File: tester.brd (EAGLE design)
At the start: 56 x 67 mm, 71 parts, among them IC1 ATmega8/88/168, K1 NA 05W K, M1 SP6000C-180, P1 250, P2 10k lin, Q1 BC847CSMD, Q2 BC847CSMD, Q3 BC807-40SMD, Q4 8,000 MHz, Q5 BC847CSMD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

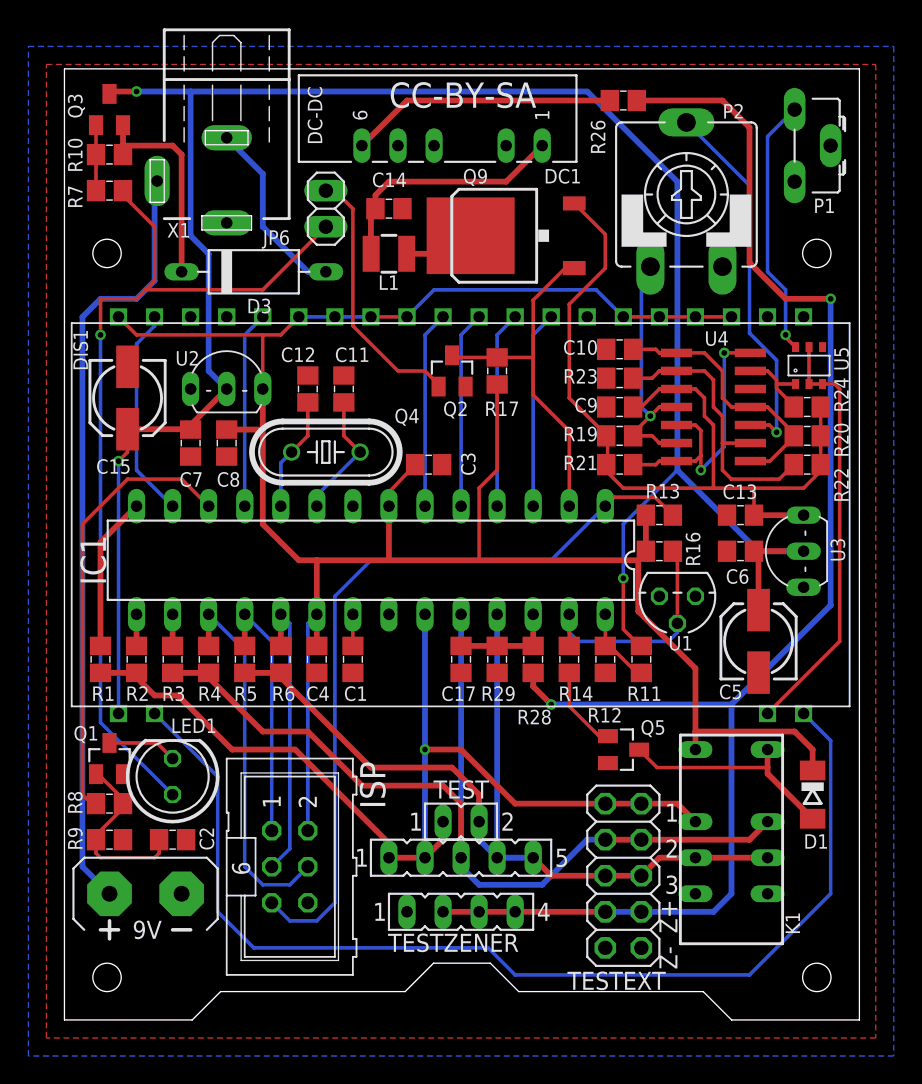
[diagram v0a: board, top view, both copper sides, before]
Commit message: continous part names/numbers
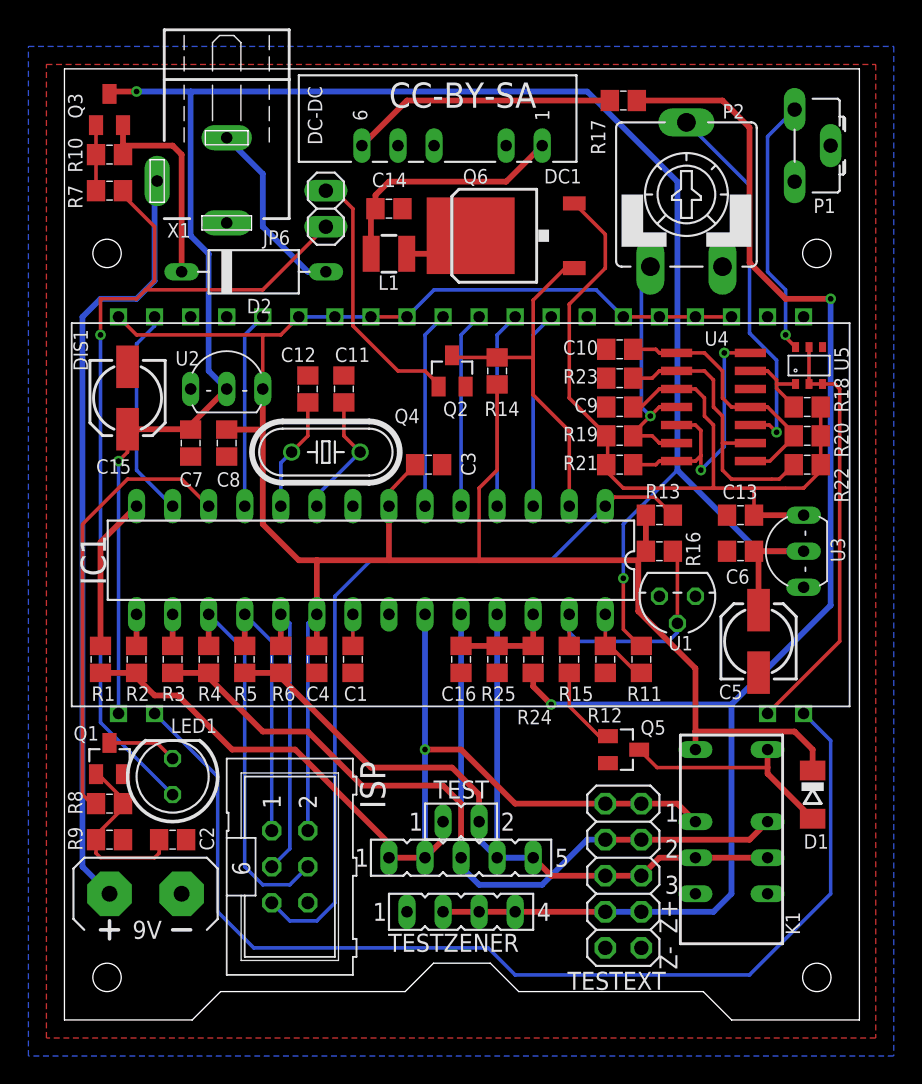
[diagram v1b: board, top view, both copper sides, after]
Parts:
- removed R26: 10k, resistor:R0805
- removed R28: 180k, resistor:R0805
- added R15: 4k7, resistor:R0805
- added R18: 3k3, resistor:R0805
- R14: value 4k7 -> 27k
- R17: value 27k -> 10k
- R24: value 3k3 -> 180k
- moved R24 26.2 mm to (33.0, 25.4), turned to 270 degrees
- moved R17 21.0 mm to (39.4, 64.8), turned to 0 degrees
- moved R14 20.9 mm to (30.5, 45.7)
- renumbered C17 to C16, D3 to D2, Q9 to Q6, R29 to R25
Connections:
- net +30V: now also R17.2, R24.2; no longer R26.2, R28.2
- net +5V: now also R14.2; no longer R17.2
- net +5V/2: now also R18.2; no longer R24.2
- net N$17: now also R18.1; no longer R24.1
- net N$22: now also R15.2; no longer R14.2
- net N$28: now also R17.1; no longer R26.1
- net PC3: now also R24.1; no longer R28.1
- net PC4: now also R15.1; no longer R14.1
- net PD0: now also R14.1; no longer R17.1
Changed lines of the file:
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@@
 <layer number="44" name="Drills" color="7" fill="1" visible="yes" active="yes"/>
 <layer number="45" name="Holes" color="7" fill="1" visible="yes" active="yes"/>
-<layer number="46" name="Milling" color="3" fill="1" visible="no" active="yes"/>
+<layer number="46" name="Milling" color="3" fill="1" visible="yes" active="yes"/>
 <layer number="47" name="Measures" color="7" fill="1" visible="no" active="yes"/>
 <layer number="48" name="Document" color="7" fill="1" visible="no" active="yes"/>
@@
 <attribute name="VALUE" x="8.89" y="41.148" size="1.27" layer="27" ratio="10"/>
 </element>
-<element name="R17" library="resistor" package="R0805" value="27k" x="30.48" y="45.72" smashed="yes" rot="R270">
+<element name="R14" library="resistor" package="R0805" value="27k" x="30.48" y="45.72" smashed="yes" rot="R270">
 <attribute name="NAME" x="29.591" y="42.545" size="1.016" layer="25"/>
 <attribute name="VALUE" x="28.448" y="46.609" size="1.27" layer="27" rot="R270"/>
@@
 <attribute name="VALUE" x="-0.635" y="65.913" size="1.27" layer="27" ratio="10"/>
 </element>
-<element name="D3" library="markus" package="DIODE-3-10" value="SB130" x="13.335" y="52.705" smashed="yes">
+<element name="D2" library="markus" package="DIODE-3-10" value="SB130" x="13.335" y="52.705" smashed="yes">
 <attribute name="NAME" x="14.605" y="50.8" size="1.016" layer="25" rot="R180"/>
 <attribute name="VALUE" x="8.89" y="53.34" size="1.27" layer="27" ratio="10"/>
@@
 <variant name="nopwm" populate="no"/>
 </element>
-<element name="R24" library="resistor" package="R0805" value="3k3" x="52.324" y="43.18" smashed="yes">
+<element name="R18" library="resistor" package="R0805" value="3k3" x="52.324" y="43.18" smashed="yes">
 <attribute name="NAME" x="55.245" y="42.799" size="1.016" layer="25" rot="R90"/>
 <attribute name="VALUE" x="51.435" y="41.148" size="1.27" layer="27"/>
@@
 <attribute name="VALUE" x="36.211" y="20.948" size="1.27" layer="27" rot="R270"/>
 </element>
-<element name="R14" library="resistor" package="R0805" value="4k7" x="35.56" y="25.4" smashed="yes" rot="R270">
+<element name="R15" library="resistor" package="R0805" value="4k7" x="35.56" y="25.4" smashed="yes" rot="R270">
 <attribute name="NAME" x="34.798" y="22.479" size="1.016" layer="25"/>
 <attribute name="VALUE" x="33.528" y="26.289" size="1.27" layer="27" rot="R270"/>
@@
 <attribute name="VALUE" x="52.07" y="24.765" size="1.016" layer="27" rot="R90"/>
 </element>
-<element name="Q9" library="transistor-power" package="D-PAK_TO252AA" value="IRFR9024" x="31.115" y="55.245" smashed="yes" rot="R90">
+<element name="Q6" library="transistor-power" package="D-PAK_TO252AA" value="IRFR9024" x="31.115" y="55.245" smashed="yes" rot="R90">
 <attribute name="NAME" x="28.067" y="58.928" size="1.016" layer="25"/>
 <attribute name="VALUE" x="33.655" y="60.325" size="1.27" layer="27" rot="R180"/>
@@
 <attribute name="VALUE" x="23.368" y="62.865" size="1.27" layer="27" ratio="10"/>
 </element>
-<element name="R26" library="resistor" package="R0805" value="10k" x="39.37" y="64.77" smashed="yes">
+<element name="R17" library="resistor" package="R0805" value="10k" x="39.37" y="64.77" smashed="yes">
 <attribute name="NAME" x="38.1" y="60.96" size="1.016" layer="25" rot="R90"/>
 <attribute name="VALUE" x="38.481" y="62.738" size="1.27" layer="27"/>
 </element>
-<element name="R28" library="resistor" package="R0805" value="180k" x="33.02" y="25.4" smashed="yes" rot="R270">
+<element name="R24" library="resistor" package="R0805" value="180k" x="33.02" y="25.4" smashed="yes" rot="R270">
 <attribute name="TOLERANCE" value="0.1%" x="33.02" y="25.4" size="1.778" layer="27" rot="R270" display="off"/>
 <attribute name="NAME" x="31.877" y="20.828" size="1.016" layer="25"/>
 <attribute name="VALUE" x="30.988" y="26.289" size="1.27" layer="27" rot="R270"/>
 </element>
-<element name="R29" library="resistor" package="R0805" value="20k" x="30.48" y="25.4" smashed="yes" rot="R90">
+<element name="R25" library="resistor" package="R0805" value="20k" x="30.48" y="25.4" smashed="yes" rot="R90">
 <attribute name="TOLERANCE" value="0.1%" x="30.48" y="25.4" size="1.778" layer="27" rot="R90" display="off"/>
 <attribute name="NAME" x="29.337" y="22.479" size="1.016" layer="25"/>
 <attribute name="VALUE" x="32.512" y="24.511" size="1.27" layer="27" rot="R90"/>
 </element>
-<element name="C17" library="rcl" package="C0805" value="10n" x="27.94" y="25.4" smashed="yes" rot="R270">
+<element name="C16" library="rcl" package="C0805" value="10n" x="27.94" y="25.4" smashed="yes" rot="R270">
 <attribute name="NAME" x="26.543" y="22.479" size="1.016" layer="25"/>
 <attribute name="VALUE" x="26.035" y="26.035" size="1.27" layer="27" rot="R270"/>
@@
 <contactref element="C13" pad="2"/>
 <contactref element="C6" pad="2"/>
-<contactref element="R29" pad="1"/>
-<contactref element="C17" pad="2"/>
+<contactref element="R25" pad="1"/>
+<contactref element="C16" pad="2"/>
 <contactref element="JP3" pad="1"/>
 <contactref element="U5" pad="4"/>
@@
 <contactref element="R10" pad="1"/>
 <contactref element="Q3" pad="E"/>
-<contactref element="D3" pad="C"/>
+<contactref element="D2" pad="C"/>
 <wire x1="8.255" y1="52.705" x2="8.255" y2="60.96" width="0.4064" layer="1"/>
 <wire x1="3.81" y1="60.96" x2="4.125" y2="60.96" width="0.4064" layer="1"/>
@@
 <signal name="+5V">
 <contactref element="JP1" pad="2"/>
-<contactref element="R17" pad="2"/>
+<contactref element="R14" pad="2"/>
 <contactref element="C3" pad="2"/>
 <contactref element="R13" pad="1"/>
@@
 </signal>
 <signal name="N$11">
-<contactref element="D3" pad="A"/>
+<contactref element="D2" pad="A"/>
 <contactref element="X1" pad="3"/>
 <wire x1="13.97" y1="59.61" x2="13.97" y2="55.88" width="0.4064" layer="16"/>
@@
 </signal>
 <signal name="N$17">
-<contactref element="R24" pad="1"/>
+<contactref element="R18" pad="1"/>
 <contactref element="U4" pad="13"/>
 <contactref element="U5" pad="1"/>
@@
 </signal>
 <signal name="PC4">
-<contactref element="R14" pad="1"/>
+<contactref element="R15" pad="1"/>
 <contactref element="R16" pad="1"/>
 <contactref element="U1" pad="2"/>
@@
 </signal>
 <signal name="N$22">
-<contactref element="R14" pad="2"/>
+<contactref element="R15" pad="2"/>
 <contactref element="Q5" pad="1"/>
 <wire x1="35.56" y1="24.45" x2="35.56" y2="22.103" width="0.254" layer="1"/>
@@
 </signal>
 <signal name="PC3">
-<contactref element="R29" pad="2"/>
-<contactref element="C17" pad="1"/>
-<contactref element="R28" pad="1"/>
+<contactref element="R25" pad="2"/>
+<contactref element="C16" pad="1"/>
+<contactref element="R24" pad="1"/>
 <contactref element="IC1" pad="26"/>
 <wire x1="30.48" y1="26.35" x2="33.02" y2="26.35" width="0.4064" layer="1"/>
@@
 </signal>
 <signal name="N$24">
-<contactref element="Q9" pad="4"/>
+<contactref element="Q6" pad="4"/>
 <contactref element="L1" pad="1"/>
 <wire x1="28.615" y1="55.245" x2="27.345" y2="53.975" width="0.4064" layer="1"/>
@@
 <signal name="N$28">
 <contactref element="DC1" pad="6"/>
-<contactref element="R26" pad="1"/>
+<contactref element="R17" pad="1"/>
 <wire x1="38.42" y1="64.77" x2="24.13" y2="64.77" width="0.4064" layer="1"/>
 <wire x1="24.13" y1="64.77" x2="20.955" y2="61.595" width="0.4064" layer="1"/>
 </signal>
 <signal name="+30V">
-<contactref element="R26" pad="2"/>
-<contactref element="R28" pad="2"/>
+<contactref element="R17" pad="2"/>
+<contactref element="R24" pad="2"/>
 <contactref element="JP3" pad="3"/>
 <wire x1="53.975" y1="29.21" x2="53.975" y2="50.8" width="0.4064" layer="16"/>
@@
 <contactref element="U3" pad="OUT"/>
 <contactref element="C13" pad="1"/>
-<contactref element="Q9" pad="3"/>
+<contactref element="Q6" pad="3"/>
 <contactref element="R21" pad="2"/>
 <contactref element="R20" pad="2"/>
@@
 <contactref element="R19" pad="2"/>
 <contactref element="C9" pad="1"/>
-<contactref element="R24" pad="2"/>
+<contactref element="R18" pad="2"/>
 <contactref element="U4" pad="3"/>
 <wire x1="43.12" y1="44.45" x2="41.91" y2="44.45" width="0.254" layer="1"/>
@@
 </signal>
 <signal name="PD0">
-<contactref element="R17" pad="1"/>
+<contactref element="R14" pad="1"/>
 <contactref element="Q2" pad="3"/>
 <contactref element="IC1" pad="2"/>
-<contactref element="Q9" pad="1"/>
+<contactref element="Q6" pad="1"/>
 <wire x1="35.56" y1="36.195" x2="35.56" y2="41.49" width="0.254" layer="1"/>
 <wire x1="27.555" y1="46.57" x2="27.305" y2="46.82" width="0.254" layer="1"/>

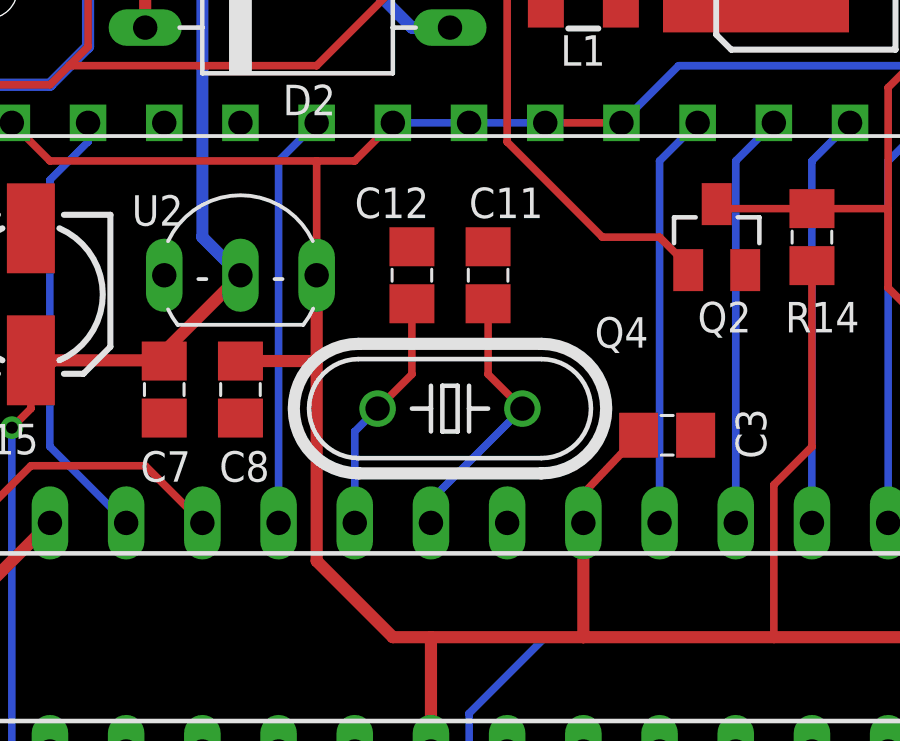
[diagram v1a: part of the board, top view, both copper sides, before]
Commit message: local oscillator gnd plane
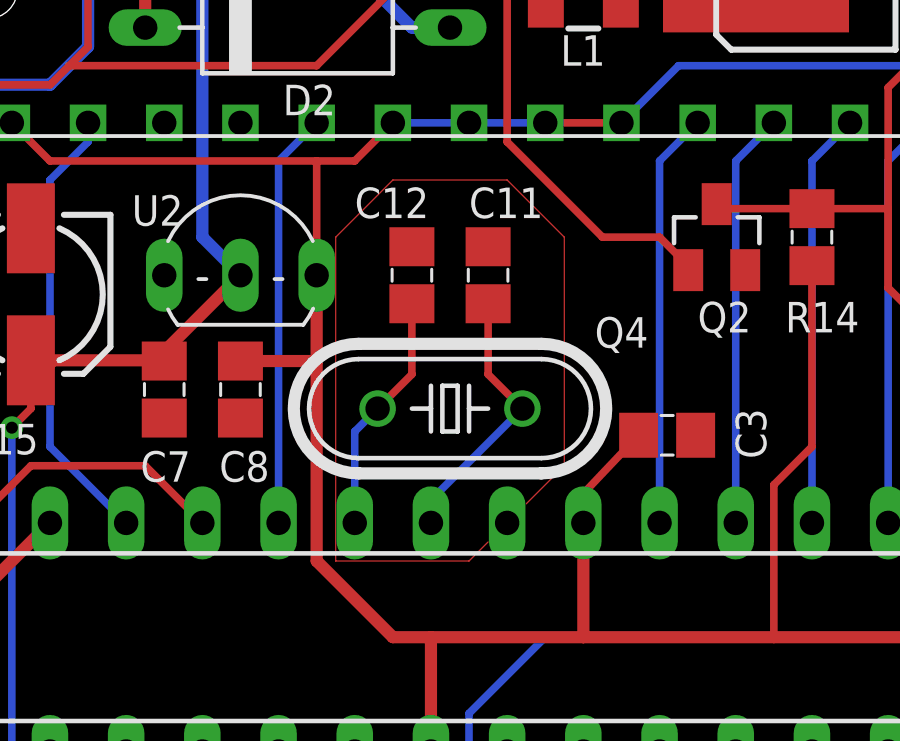
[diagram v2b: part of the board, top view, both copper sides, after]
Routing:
- net N$14: track 0.00 -> 34.8 mm
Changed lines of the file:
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@@
 <setting verticaltext="up"/>
 </settings>
-<grid distance="0.05" unitdist="inch" unit="mm" style="lines" multiple="1" display="yes" altdistance="0.025" altunitdist="inch" altunit="mm"/>
+<grid distance="0.635" unitdist="mm" unit="mm" style="lines" multiple="1" display="yes" altdistance="5" altunitdist="mil" altunit="mic"/>
 <layers>
 <layer number="1" name="Top" color="4" fill="1" visible="yes" active="yes"/>
@@
 <layer number="37" name="tTest" color="7" fill="1" visible="no" active="yes"/>
 <layer number="38" name="bTest" color="7" fill="1" visible="no" active="yes"/>
-<layer number="39" name="tKeepout" color="4" fill="11" visible="no" active="yes"/>
+<layer number="39" name="tKeepout" color="4" fill="11" visible="yes" active="yes"/>
 <layer number="40" name="bKeepout" color="1" fill="11" visible="no" active="yes"/>
 <layer number="41" name="tRestrict" color="4" fill="10" visible="yes" active="yes"/>
@@
 <wire x1="41.749" y1="17.78" x2="40.486" y2="19.043" width="0.25" layer="1"/>
 </signal>
+<signal name="N$14">
+<wire x1="19.685" y1="35.56" x2="19.05" y2="34.925" width="0" layer="1"/>
+<wire x1="19.05" y1="34.925" x2="14.605" y2="34.925" width="0" layer="1"/>
+<wire x1="14.605" y1="34.925" x2="14.605" y2="45.72" width="0" layer="1"/>
+<wire x1="14.605" y1="45.72" x2="16.51" y2="47.625" width="0" layer="1"/>
+<wire x1="16.51" y1="47.625" x2="20.32" y2="47.625" width="0" layer="1"/>
+<wire x1="20.32" y1="47.625" x2="22.225" y2="45.72" width="0" layer="1"/>
+<wire x1="22.225" y1="45.72" x2="22.225" y2="38.1" width="0" layer="1"/>
+<wire x1="22.225" y1="38.1" x2="20.955" y2="36.83" width="0" layer="1"/>
+</signal>
 </signals>

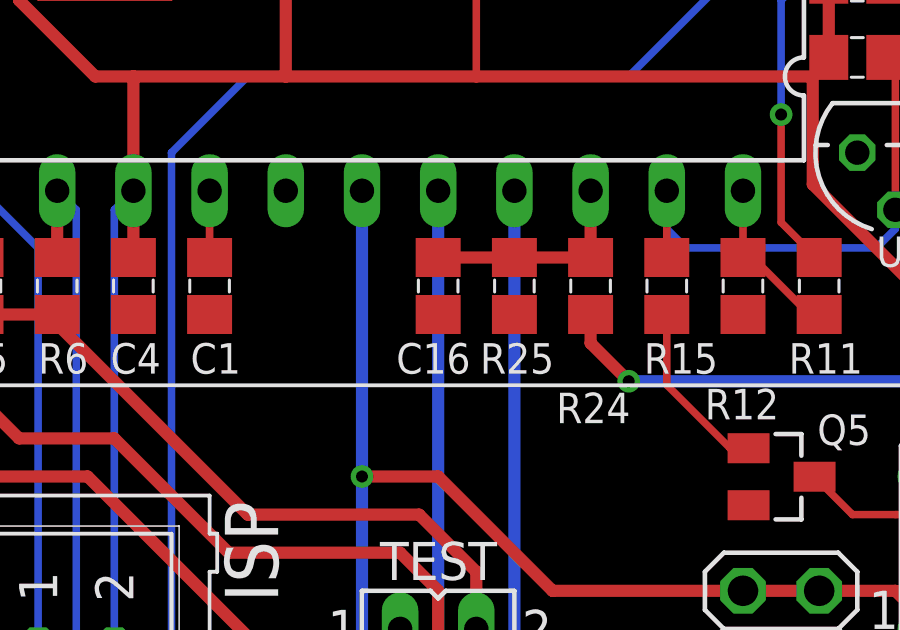
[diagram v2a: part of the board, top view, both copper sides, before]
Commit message: fix for reichelt r25 20k .1% n/a => parallel r25 22k and r26 220k
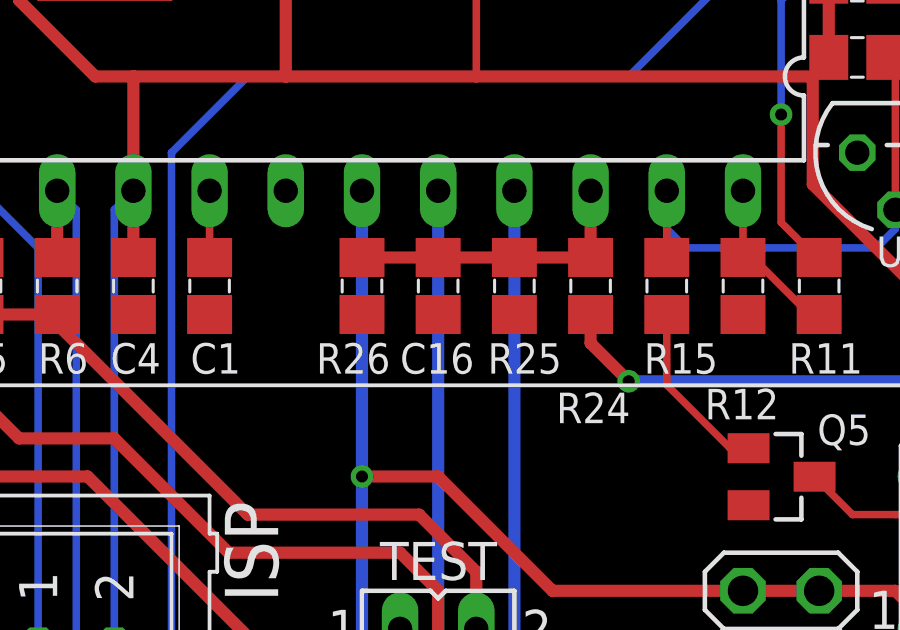
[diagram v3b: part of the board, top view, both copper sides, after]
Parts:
- added R26: inf, resistor:R0805
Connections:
- net GND: now also R26.1
- net PC3: now also R26.2
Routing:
- net PC3: track 7.45 -> 10.2 mm
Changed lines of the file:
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@@
 <variantdefs>
 <variantdef name="nopwm"/>
+<variantdef name="no20k"/>
 </variantdefs>
 <classes>
@@
 <element name="R25" library="resistor" package="R0805" value="20k" x="30.48" y="25.4" smashed="yes" rot="R90">
 <attribute name="TOLERANCE" value="0.1%" x="30.48" y="25.4" size="1.778" layer="27" rot="R90" display="off"/>
-<attribute name="NAME" x="29.337" y="22.479" size="1.016" layer="25"/>
+<attribute name="NAME" x="29.591" y="22.479" size="1.016" layer="25"/>
 <attribute name="VALUE" x="32.512" y="24.511" size="1.27" layer="27" rot="R90"/>
+<variant name="no20k" value="22k"/>
 </element>
 <element name="C16" library="rcl" package="C0805" value="10n" x="27.94" y="25.4" smashed="yes" rot="R270">
-<attribute name="NAME" x="26.543" y="22.479" size="1.016" layer="25"/>
+<attribute name="NAME" x="26.67" y="22.479" size="1.016" layer="25"/>
 <attribute name="VALUE" x="26.035" y="26.035" size="1.27" layer="27" rot="R270"/>
 </element>
@@
 <element name="JP7" library="con-lsta" package="FE02-1" value="TEST2" x="27.94" y="13.97" smashed="yes">
 <attribute name="VALUE" x="25.4" y="11.176" size="1.27" layer="27" ratio="10"/>
+</element>
+<element name="R26" library="resistor" package="R0805" value="inf" x="25.4" y="25.4" smashed="yes" rot="R90">
+<attribute name="TOLERANCE" value="0.1%" x="25.4" y="25.4" size="1.778" layer="27" rot="R90" display="off"/>
+<attribute name="NAME" x="23.876" y="22.479" size="1.016" layer="25"/>
+<attribute name="VALUE" x="27.94" y="24.13" size="1.27" layer="27" rot="R90"/>
+<variant name="no20k" value="220k"/>
 </element>
 </elements>
@@
 <contactref element="Q5" pad="2"/>
 <contactref element="P2" pad="E"/>
+<contactref element="R26" pad="1"/>
 </signal>
 <signal name="N$5">
@@
 <wire x1="28.04" y1="26.25" x2="27.94" y2="26.35" width="0.4064" layer="1"/>
 <wire x1="30.48" y1="26.35" x2="27.94" y2="26.35" width="0.4064" layer="1"/>
+<contactref element="R26" pad="2"/>
+<wire x1="28.04" y1="26.25" x2="28.04" y2="26.35" width="0.4064" layer="1"/>
+<wire x1="28.04" y1="26.35" x2="25.4" y2="26.35" width="0.4064" layer="1"/>
 </signal>
 <signal name="N$24">
